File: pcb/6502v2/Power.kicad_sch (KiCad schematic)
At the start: 8 parts

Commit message: just working
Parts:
- F1: renamed from F?; footprint (none) -> Fuse:Fuse_1206_3216Metric
- J2: renamed from J?; footprint (none) -> hooks:HRO-TYPE-C-31-M-12
- R1, R2: renamed from R?; footprint (none) -> Resistor_SMD:R_0805_2012Metric
- gave numbers to parts that had none: 4
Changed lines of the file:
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@@
   (symbol (lib_id "Device:R_Small") (at 142.875 56.515 0) (unit 1)
     (in_bom yes) (on_board yes) (fields_autoplaced)
-    (property "Reference" "R?" (id 0) (at 145.415 55.2449 0)
+    (property "Reference" "R3" (id 0) (at 145.415 55.2449 0)
       (effects (font (size 1.27 1.27)) (justify left))
     )
@@
   (symbol (lib_id "Device:Polyfuse_Small") (at 115.57 35.56 90) (unit 1)
     (in_bom yes) (on_board yes) (fields_autoplaced)
-    (property "Reference" "F?" (id 0) (at 115.57 29.845 90))
+    (property "Reference" "F1" (id 0) (at 115.57 29.845 90))
     (property "Value" "Polyfuse_Small" (id 1) (at 115.57 32.385 90))
-    (property "Footprint" "" (id 2) (at 120.65 34.29 0)
+    (property "Footprint" "Fuse:Fuse_1206_3216Metric" (id 2) (at 120.65 34.29 0)
       (effects (font (size 1.27 1.27)) (justify left) hide)
     )
@@
   (symbol (lib_id "Device:R_Small") (at 90.17 50.8 0) (unit 1)
     (in_bom yes) (on_board yes) (fields_autoplaced)
-    (property "Reference" "R?" (id 0) (at 92.71 49.5299 0)
+    (property "Reference" "R2" (id 0) (at 92.71 49.5299 0)
       (effects (font (size 1.27 1.27)) (justify left))
     )
@@
       (effects (font (size 1.27 1.27)) (justify left))
     )
-    (property "Footprint" "" (id 2) (at 90.17 50.8 0)
+    (property "Footprint" "Resistor_SMD:R_0805_2012Metric" (id 2) (at 90.17 50.8 0)
       (effects (font (size 1.27 1.27)) hide)
     )
@@
   (symbol (lib_id "power:+5V") (at 142.875 43.815 0) (unit 1)
     (in_bom yes) (on_board yes) (fields_autoplaced)
-    (property "Reference" "#PWR0104" (id 0) (at 142.875 47.625 0)
+    (property "Reference" "#PWR020" (id 0) (at 142.875 47.625 0)
       (effects (font (size 1.27 1.27)) hide)
     )
@@
   (symbol (lib_id "Connector:USB_C_Receptacle") (at 56.515 66.04 0) (unit 1)
     (in_bom yes) (on_board yes) (fields_autoplaced)
-    (property "Reference" "J?" (id 0) (at 56.515 33.02 0))
+    (property "Reference" "J2" (id 0) (at 56.515 33.02 0))
     (property "Value" "USB_C_Receptacle" (id 1) (at 56.515 35.56 0))
-    (property "Footprint" "" (id 2) (at 60.325 66.04 0)
+    (property "Footprint" "hooks:HRO-TYPE-C-31-M-12" (id 2) (at 60.325 66.04 0)
       (effects (font (size 1.27 1.27)) hide)
     )
@@
   (symbol (lib_id "power:GND") (at 84.455 55.245 0) (unit 1)
     (in_bom yes) (on_board yes) (fields_autoplaced)
-    (property "Reference" "#PWR0115" (id 0) (at 84.455 61.595 0)
+    (property "Reference" "#PWR013" (id 0) (at 84.455 61.595 0)
       (effects (font (size 1.27 1.27)) hide)
     )
@@
   (symbol (lib_id "power:GND") (at 142.875 59.055 0) (unit 1)
     (in_bom yes) (on_board yes) (fields_autoplaced)
-    (property "Reference" "#PWR0105" (id 0) (at 142.875 65.405 0)
+    (property "Reference" "#PWR021" (id 0) (at 142.875 65.405 0)
       (effects (font (size 1.27 1.27)) hide)
     )
@@
   (symbol (lib_id "Switch:SW_SPST") (at 102.235 35.56 0) (unit 1)
     (in_bom yes) (on_board yes) (fields_autoplaced)
-    (property "Reference" "SW?" (id 0) (at 102.235 29.21 0))
+    (property "Reference" "SW1" (id 0) (at 102.235 29.21 0))
     (property "Value" "SW_SPST" (id 1) (at 102.235 31.75 0))
     (property "Footprint" "" (id 2) (at 102.235 35.56 0)
@@
   (symbol (lib_id "power:GND") (at 106.045 83.82 0) (unit 1)
     (in_bom yes) (on_board yes) (fields_autoplaced)
-    (property "Reference" "#PWR0121" (id 0) (at 106.045 90.17 0)
+    (property "Reference" "#PWR016" (id 0) (at 106.045 90.17 0)
       (effects (font (size 1.27 1.27)) hide)
     )
@@
   (symbol (lib_id "power:GND") (at 56.515 108.585 0) (unit 1)
     (in_bom yes) (on_board yes) (fields_autoplaced)
-    (property "Reference" "#PWR0109" (id 0) (at 56.515 114.935 0)
+    (property "Reference" "#PWR011" (id 0) (at 56.515 114.935 0)
       (effects (font (size 1.27 1.27)) hide)
     )
@@
   (symbol (lib_id "Device:R_Small") (at 78.74 50.8 0) (unit 1)
     (in_bom yes) (on_board yes) (fields_autoplaced)
-    (property "Reference" "R?" (id 0) (at 81.28 49.5299 0)
+    (property "Reference" "R1" (id 0) (at 81.28 49.5299 0)
       (effects (font (size 1.27 1.27)) (justify left))
     )
@@
       (effects (font (size 1.27 1.27)) (justify left))
     )
-    (property "Footprint" "" (id 2) (at 78.74 50.8 0)
+    (property "Footprint" "Resistor_SMD:R_0805_2012Metric" (id 2) (at 78.74 50.8 0)
       (effects (font (size 1.27 1.27)) hide)
     )
@@
   (symbol (lib_id "Connector:Barrel_Jack") (at 111.76 55.245 0) (unit 1)
     (in_bom yes) (on_board yes) (fields_autoplaced)
-    (property "Reference" "J?" (id 0) (at 111.76 46.355 0))
+    (property "Reference" "J3" (id 0) (at 111.76 46.355 0))
     (property "Value" "Barrel_Jack" (id 1) (at 111.76 48.895 0))
     (property "Footprint" "Connector_BarrelJack:BarrelJack_GCT_DCJ200-10-A_Horizontal" (id 2) (at 113.03 56.261 0)
@@
   (symbol (lib_id "power:VCC") (at 88.265 35.56 0) (unit 1)
     (in_bom yes) (on_board yes) (fields_autoplaced)
-    (property "Reference" "#PWR0111" (id 0) (at 88.265 39.37 0)
+    (property "Reference" "#PWR014" (id 0) (at 88.265 39.37 0)
       (effects (font (size 1.27 1.27)) hide)
     )
@@
   (symbol (lib_id "Device:LED_Small") (at 142.875 48.895 90) (unit 1)
     (in_bom yes) (on_board yes) (fields_autoplaced)
-    (property "Reference" "D?" (id 0) (at 145.415 47.5614 90)
+    (property "Reference" "D1" (id 0) (at 145.415 47.5614 90)
       (effects (font (size 1.27 1.27)) (justify right))
     )
@@
   (symbol (lib_id "power:+5V") (at 127 35.56 0) (unit 1)
     (in_bom yes) (on_board yes) (fields_autoplaced)
-    (property "Reference" "#PWR0114" (id 0) (at 127 39.37 0)
+    (property "Reference" "#PWR019" (id 0) (at 127 39.37 0)
       (effects (font (size 1.27 1.27)) hide)
     )
@@
   (symbol (lib_id "power:+5V") (at 106.045 79.375 0) (unit 1)
     (in_bom yes) (on_board yes) (fields_autoplaced)
-    (property "Reference" "#PWR0116" (id 0) (at 106.045 83.185 0)
+    (property "Reference" "#PWR015" (id 0) (at 106.045 83.185 0)
       (effects (font (size 1.27 1.27)) hide)
     )
@@
   (symbol (lib_id "power:VCC") (at 74.295 40.64 0) (unit 1)
     (in_bom yes) (on_board yes) (fields_autoplaced)
-    (property "Reference" "#PWR0110" (id 0) (at 74.295 44.45 0)
+    (property "Reference" "#PWR012" (id 0) (at 74.295 44.45 0)
       (effects (font (size 1.27 1.27)) hide)
     )
@@
   (symbol (lib_id "power:GND") (at 124.46 57.785 0) (unit 1)
     (in_bom yes) (on_board yes) (fields_autoplaced)
-    (property "Reference" "#PWR0106" (id 0) (at 124.46 64.135 0)
+    (property "Reference" "#PWR018" (id 0) (at 124.46 64.135 0)
       (effects (font (size 1.27 1.27)) hide)
     )
@@
   (symbol (lib_id "power:VCC") (at 124.46 52.705 0) (unit 1)
     (in_bom yes) (on_board yes) (fields_autoplaced)
-    (property "Reference" "#PWR0108" (id 0) (at 124.46 56.515 0)
-      (effects (font (size 1.27 1.27)) hide)
-    )
+    (property "Reference" "#PWR017" (id 0) (at 124.46 56.515 0)
+      (effects (font (size 1.27 1.27)) hide)
+    )

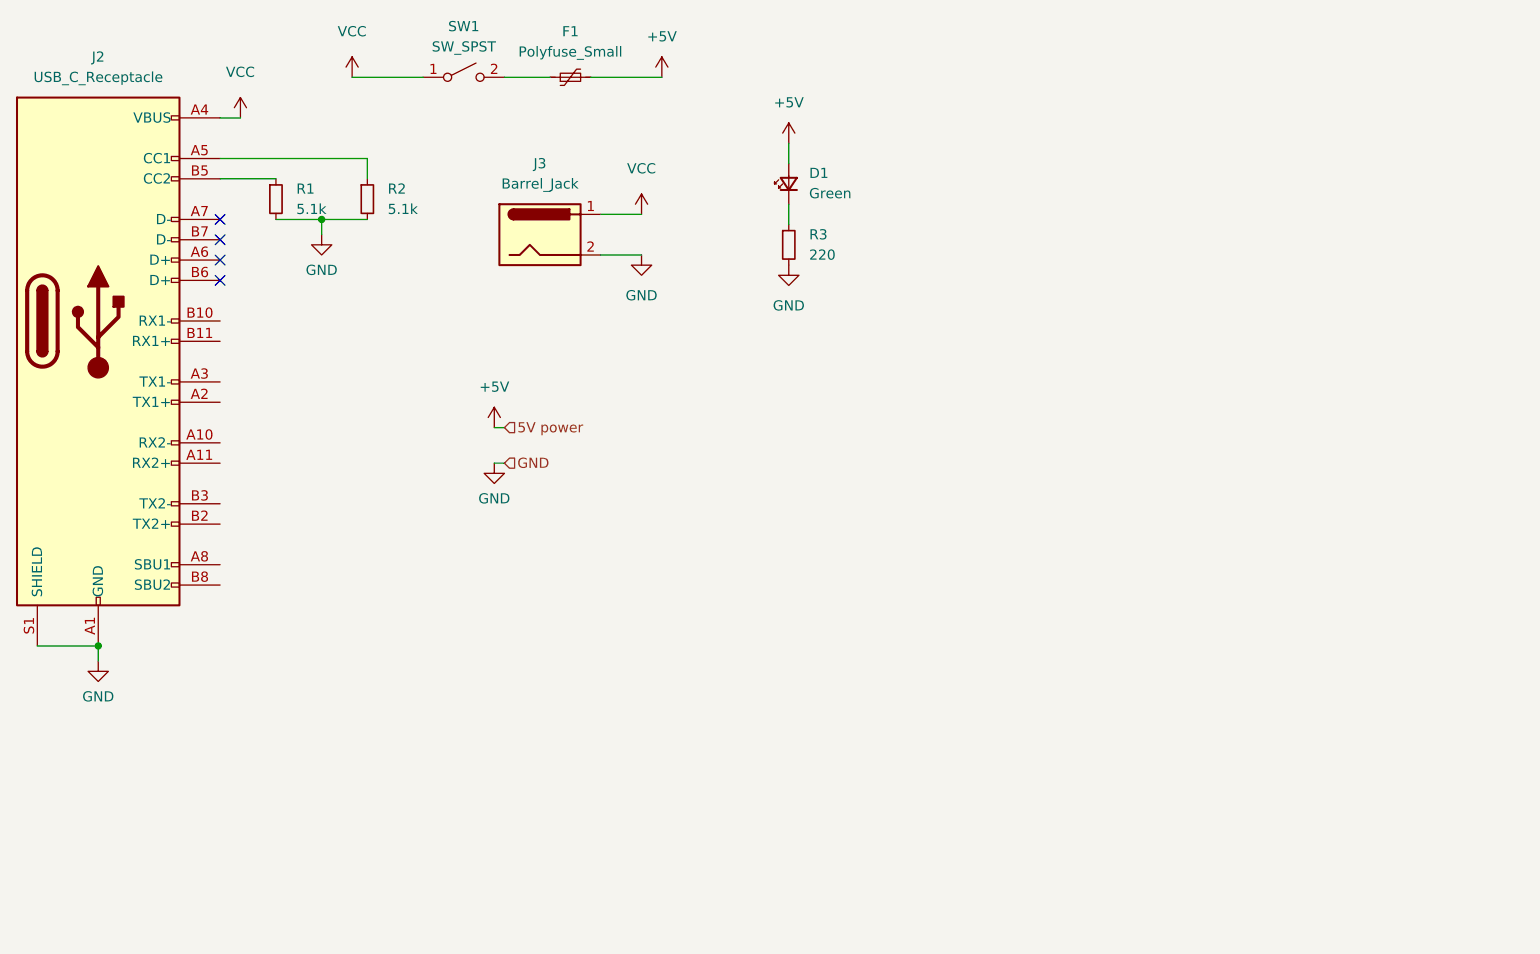
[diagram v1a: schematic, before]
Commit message: Yo yo yo i make the bord 102 by 102 cause jlc pricing
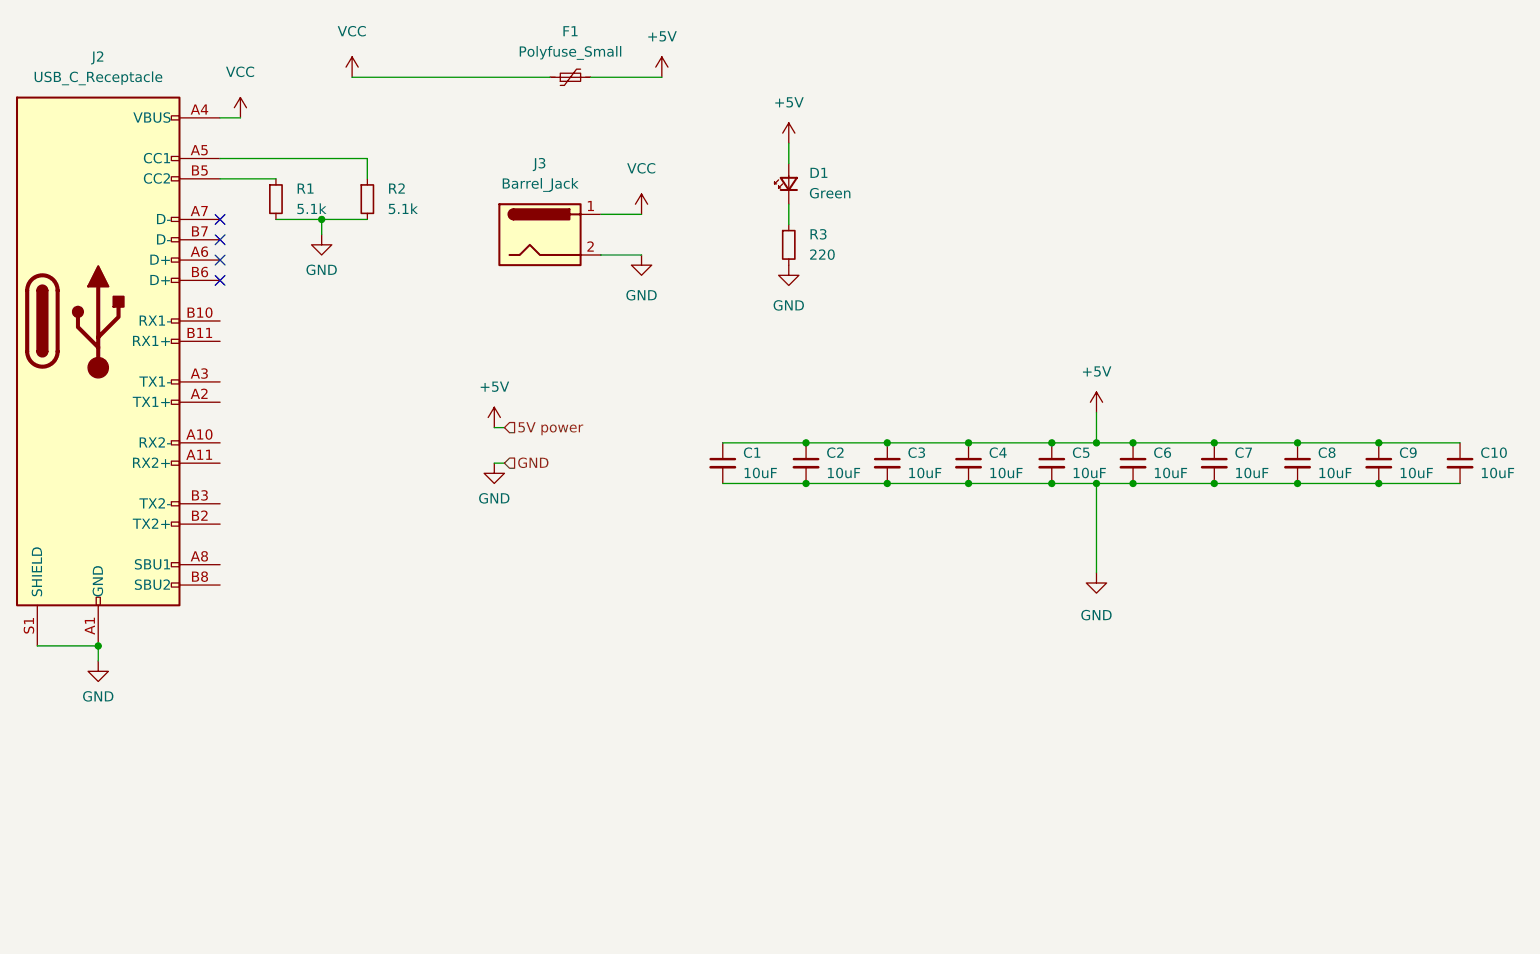
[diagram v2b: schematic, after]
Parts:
- removed SW1: SW_SPST, symbol Switch:SW_SPST
- added C1, C10, C2, C3, C4, C5, C6, C7, C8, C9: 10uF, Capacitor_SMD:C_0805_2012Metric, symbol Device:C_Small
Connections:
- net +5V: now also C1.1, C10.1, C2.1, C3.1, C4.1, C5.1, C6.1, C7.1, C8.1, C9.1
- net GND: now also C1.2, C10.2, C2.2, C3.2, C4.2, C5.2, C6.2, C7.2, C8.2, C9.2
- net VCC: now also F1.1

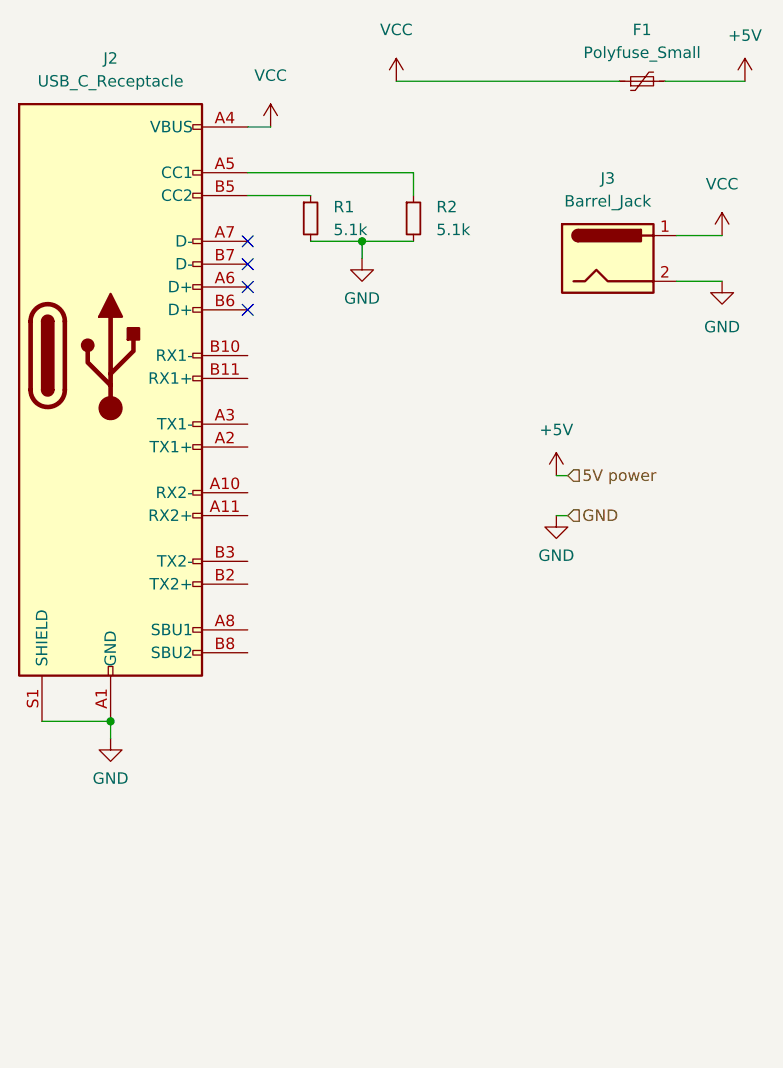
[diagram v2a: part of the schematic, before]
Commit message: First pass at routing done, now comes double checking everything
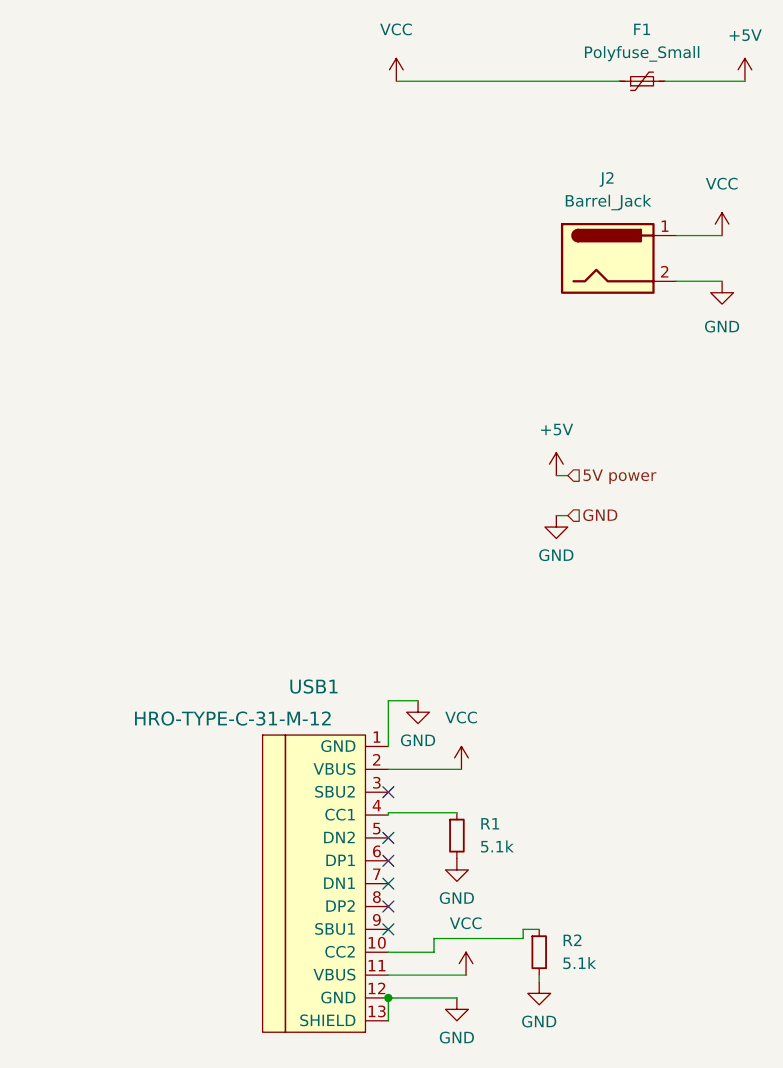
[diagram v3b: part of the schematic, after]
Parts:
- removed J2: USB_C_Receptacle, hooks:HRO-TYPE-C-31-M-12, symbol Connector:USB_C_Receptacle
- added USB1: HRO-TYPE-C-31-M-12, hooks:HRO-TYPE-C-31-M-12, symbol Type-C:HRO-TYPE-C-31-M-12
- renumbered J3 to J2
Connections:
- net GND: now also USB1.1 (GND), USB1.12 (GND), USB1.13 (SHIELD)
- net VCC: now also USB1.11 (VBUS), USB1.2 (VBUS)
- net at R2.1: now also USB1.10 (CC2)
- net at R1.1: now also USB1.4 (CC1)
- no-connect marks 4 -> 6
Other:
- moved on the sheet: R1, R2
